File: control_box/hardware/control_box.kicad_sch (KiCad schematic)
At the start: 25 parts, among them J3 SWIM, U1 L78L05, U2 STM8S003F3P

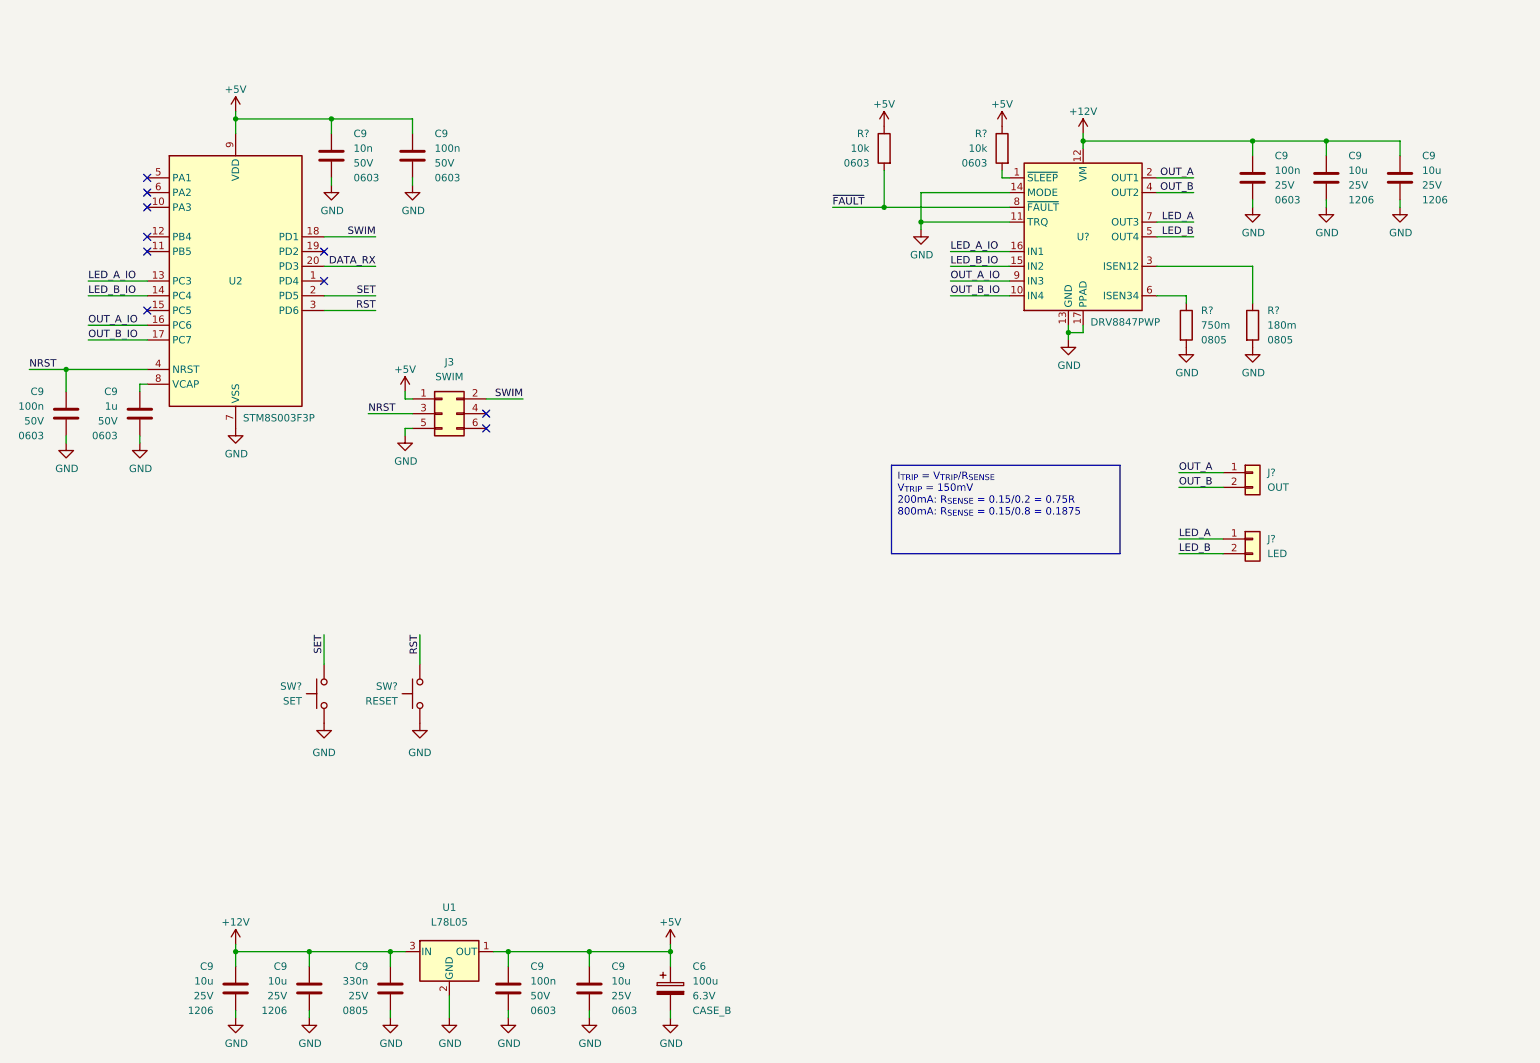
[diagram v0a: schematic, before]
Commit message: Added bufferless beam
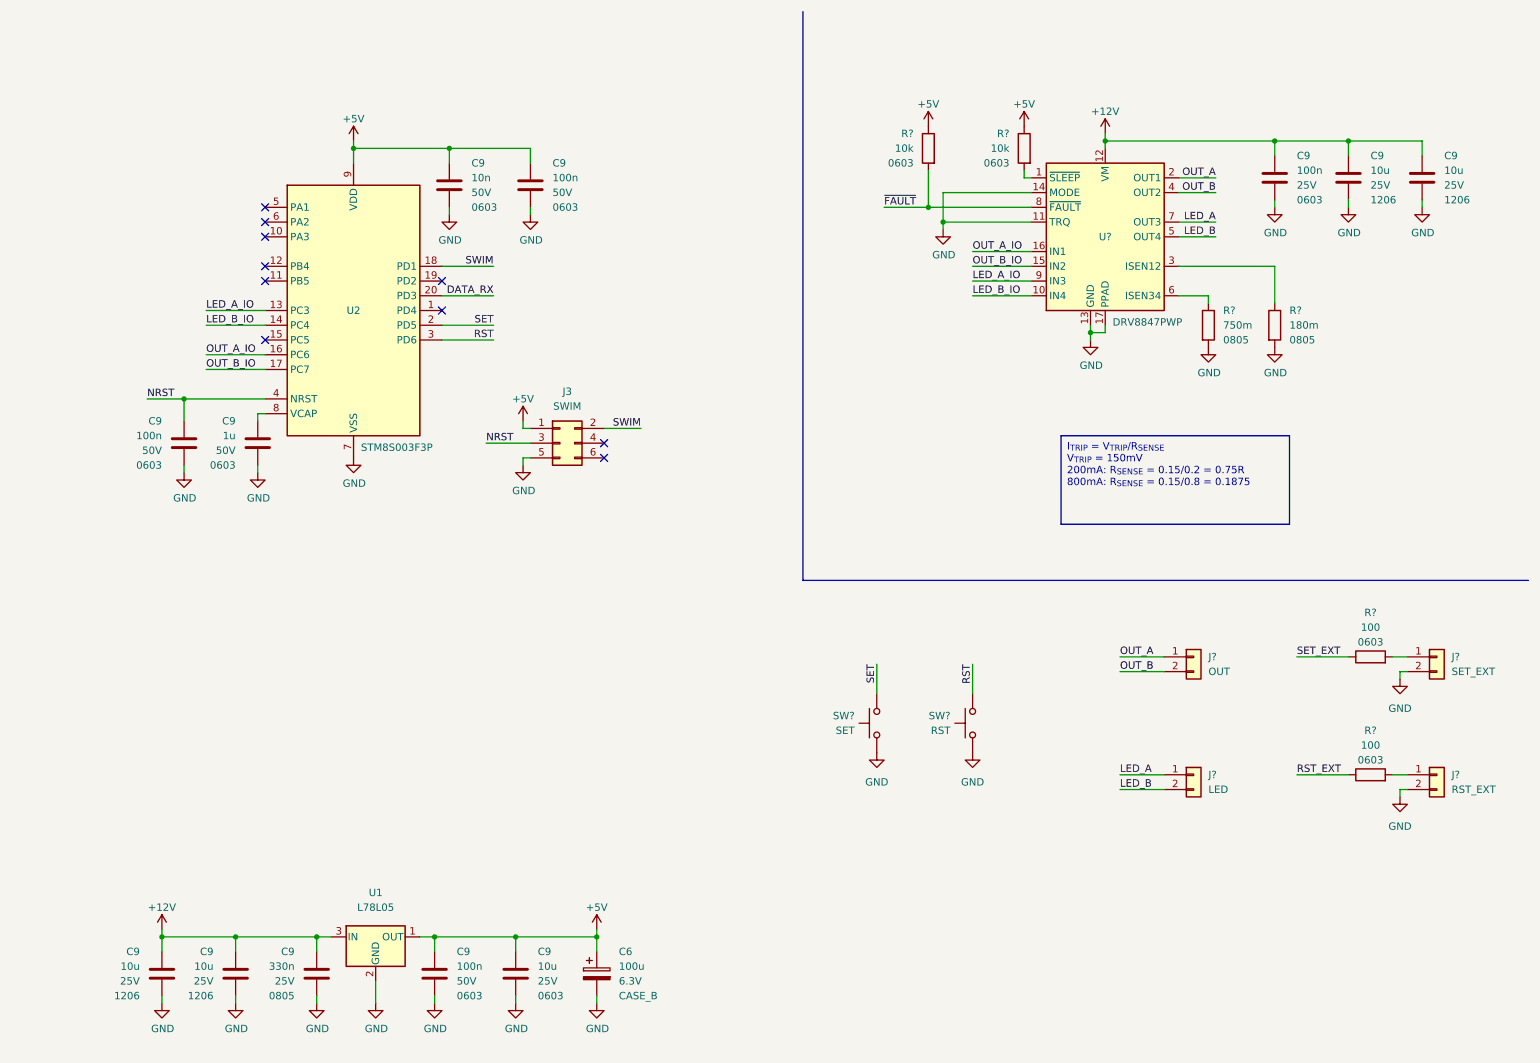
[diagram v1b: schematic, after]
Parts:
- added J?: RST_EXT, symbol Connector_Generic:Conn_01x02
- added J?: SET_EXT, symbol Connector_Generic:Conn_01x02
- added R? (x2): 100, symbol Device:R
- SW?: value RESET -> RST
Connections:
- net GND: now also J?.2 (Pin_2), J?.2 (Pin_2)
- net LED_A_IO: now also U?.9 (IN3); no longer U?.16 (IN1)
- net LED_B_IO: now also U?.10 (IN4); no longer U?.15 (IN2)
- net OUT_A_IO: now also U?.16 (IN1); no longer U?.9 (IN3)
- net OUT_B_IO: now also U?.15 (IN2); no longer U?.10 (IN4)
- new net: J?.1 (Pin_1), R?.2 (x2)
- new net RST_EXT: R?.1
- new net SET_EXT: R?.1
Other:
- moved on the sheet: C6, C9, J3, J?, R?, SW?, U1, U2, U?
